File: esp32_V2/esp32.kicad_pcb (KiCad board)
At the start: 2 copper layers, 80 x 64 mm, 75 parts, among them IC1 KF33BD-TR, J1 USB_C, J4 pH, J5 ORP, Q2 8205A, Q3 BC817, Q4 BC817, SW1 Reset, SW2 Boot, U1 CH340G, U2 TC4056, U3 DW01A, U4 LM358, U5 TLC272, U6 LM358, X1 12 MHz

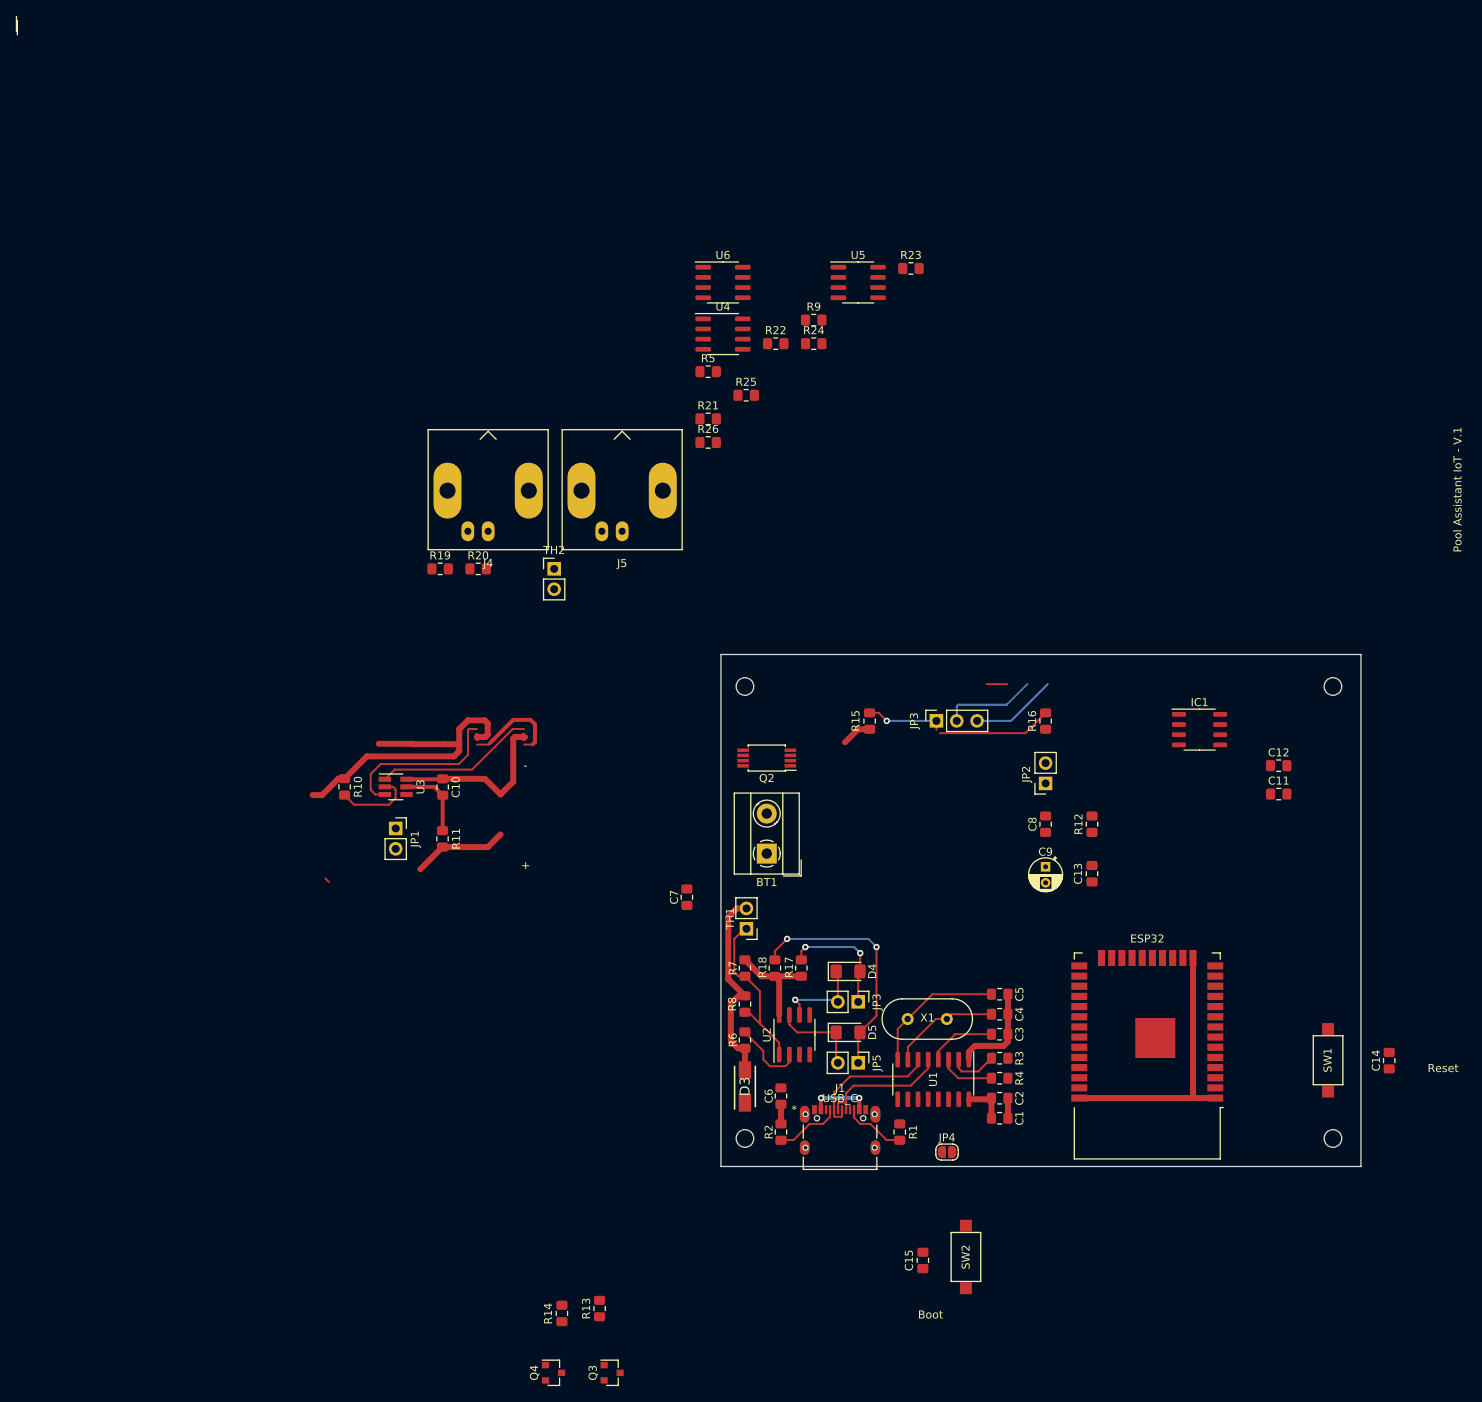
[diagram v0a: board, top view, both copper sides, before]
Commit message: Remove V2 folder and rename V2.1 folder to V2
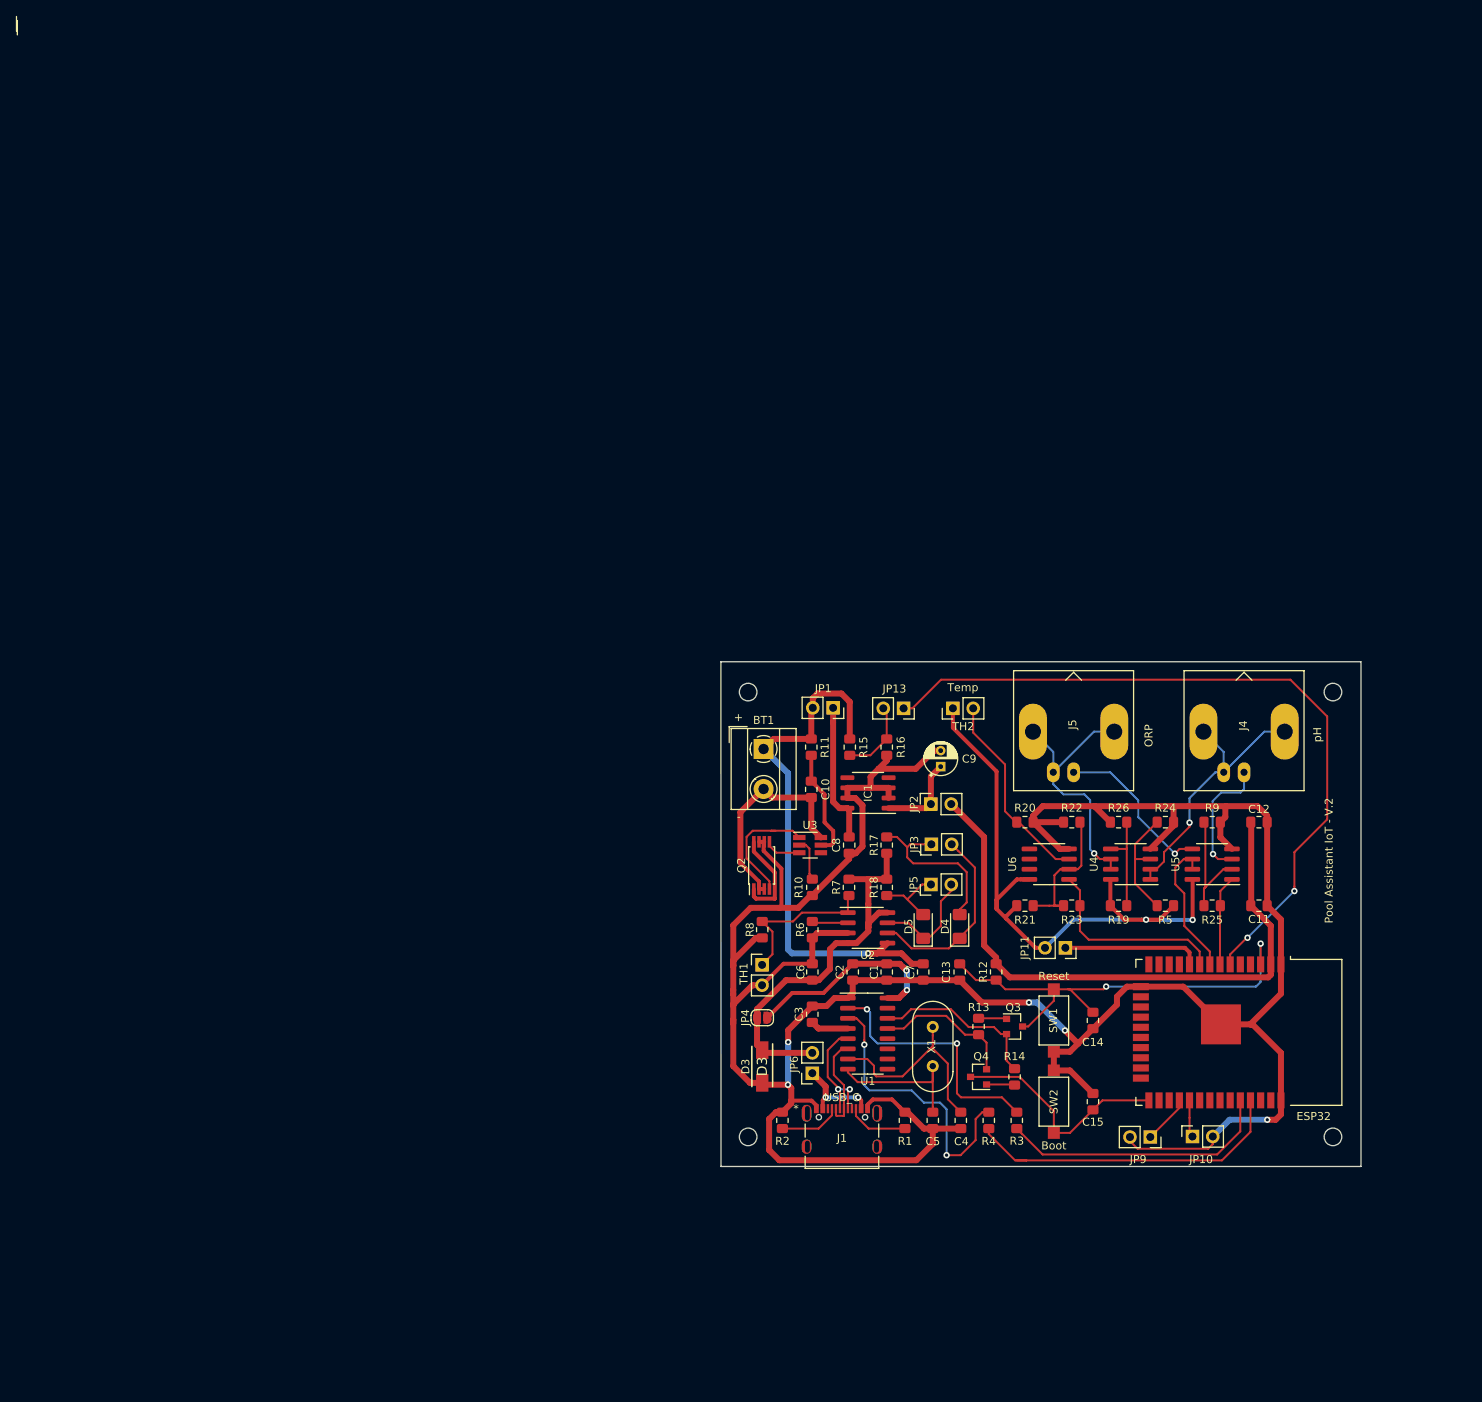
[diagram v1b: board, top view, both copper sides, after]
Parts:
- removed Hole1, Hole3, Hole4: MountingHole_2.2mm_M2_ISO7380, MountingHole:MountingHole_2.2mm_M2_ISO7380
- removed the Hole2 at (164.5, 83.0)
- removed the JP3 at (105.2, 122.4)
- removed the JP3 at (114.9, 87.3)
- added Hole2: MountingHole_2.2mm_M2_ISO7380, MountingHole:MountingHole_2.2mm_M2_ISO7380, F.Cu at (164.5, 83.7)
- added Hole2: MountingHole_2.2mm_M2_ISO7380, MountingHole:MountingHole_2.2mm_M2_ISO7380, F.Cu at (164.5, 139.3)
- added Hole2: MountingHole_2.2mm_M2_ISO7380, MountingHole:MountingHole_2.2mm_M2_ISO7380, F.Cu at (91.4, 139.3)
- added Hole2: MountingHole_2.2mm_M2_ISO7380, MountingHole:MountingHole_2.2mm_M2_ISO7380, F.Cu at (91.4, 83.7)
- added JP10: Jumper_NO, Connector_PinSocket_2.54mm:PinSocket_1x02_P2.54mm_Vertical, F.Cu at (146.9, 139.3)
- added JP11: Jumper_NO, Connector_PinSocket_2.54mm:PinSocket_1x02_P2.54mm_Vertical, F.Cu at (131.1, 115.7)
- added JP13: Jumper_NO, Connector_PinSocket_2.54mm:PinSocket_1x02_P2.54mm_Vertical, F.Cu at (110.8, 85.7)
- added JP3: READY, Connector_PinHeader_2.54mm:PinHeader_1x02_P2.54mm_Vertical, F.Cu at (114.3, 102.7)
- added JP6: Jumper_NO, Connector_PinSocket_2.54mm:PinSocket_1x02_P2.54mm_Vertical, F.Cu at (99.4, 131.3)
- added JP9: Jumper_NO, Connector_PinSocket_2.54mm:PinSocket_1x02_P2.54mm_Vertical, F.Cu at (141.7, 139.3)
- moved J4 99.2 mm to (153.4, 93.7)
- moved R19 94.7 mm to (137.7, 110.4), turned to 180 degrees
- moved R5 87.9 mm to (143.6, 110.4)
- moved R25 86.4 mm to (149.4, 110.4)
- moved U5 85.1 mm to (149.4, 105.2), turned to 180 degrees
- moved U4 83.6 mm to (139.2, 105.2), turned to 180 degrees
- moved U6 83.4 mm to (129.0, 105.2), turned to 180 degrees
- moved R23 82.1 mm to (131.8, 110.4), turned to 180 degrees
- moved R9 80.1 mm to (149.4, 100.0), turned to 180 degrees
- moved R20 75.3 mm to (126.0, 100.0), turned to 180 degrees
- moved R24 74.2 mm to (143.6, 100.0)
- moved R21 72.6 mm to (126.0, 110.4)
- moved R22 70.3 mm to (131.8, 100.0), turned to 180 degrees
- moved R26 69.9 mm to (137.7, 100.0), turned to 180 degrees
- moved G*** 67.0 mm to (151.9, 123.0)
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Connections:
- ESP32 pad 10: Vcc -> Net-(ESP32-Pad10)
- ESP32 pad 6: pH -> Bat
- ESP32 pad 7: Temp -> pH
- ESP32 pad 9: Bat -> Temp
- J1 pad A4-B9: VBUS -> Net-(J1-PadA4-B9)
- J1 pad B4-A9: VBUS -> Net-(J1-PadA4-B9)
- R15 pad 2: Bat -> Net-(JP13-Pad2)
- R16 pad 1: Bat -> Net-(JP13-Pad2)
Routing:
- net GND: track 119.0 -> 370.6 mm, vias 0 -> 5
- net Vcc: track 0.00 -> 81.5 mm, vias 0 -> 2
- net Bat: track 14.3 -> 92.4 mm, vias 0 -> 2
- net +3V3: track 0.00 -> 77.6 mm
- net EN: track 0.00 -> 57.7 mm, vias 0 -> 2
- net Batt+: track 15.6 -> 68.7 mm, vias 0 -> 1
- net Tx: track 0.00 -> 41.4 mm
- net Rx: track 0.00 -> 34.3 mm
- net pH-: track 0.00 -> 34.1 mm, vias 0 -> 1
- net ORP-: track 0.00 -> 33.3 mm, vias 0 -> 1
- net Net-(R4-Pad2): track 6.98 -> 36.2 mm, vias 0 -> 2
- net Boot: track 0.00 -> 28.5 mm
- net VBUS: track 20.7 -> 49.1 mm, vias 2 -> 0
- net Net-(R3-Pad2): track 6.02 -> 31.9 mm, vias 0 -> 2
- net Net-(R20-Pad2): track 0.00 -> 25.0 mm
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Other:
- board size 80 x 64 mm -> 80 x 63.1 mm
- board text added: "D3"
- board text added: "ORP"
- board text added: "Pool Assistant IoT - V.2"
- board text added: "Temp"
- board text added: "pH"
- board text removed: "Pool Assistant IoT - V.1"

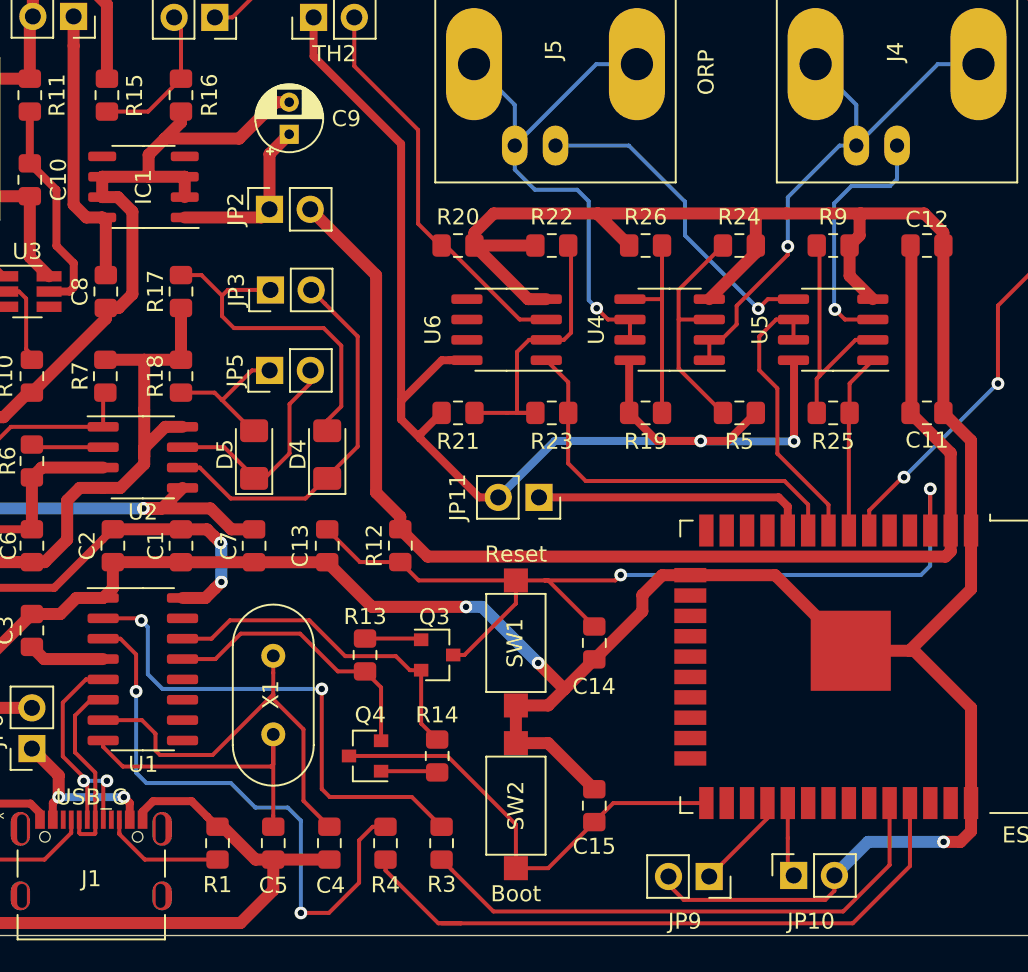
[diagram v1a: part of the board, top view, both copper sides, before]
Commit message: 1) Correct components values in measurement circuits - 2) Schematic cleanup - 3) Fix tracks in PCB - 4) Add Thermistor calculator
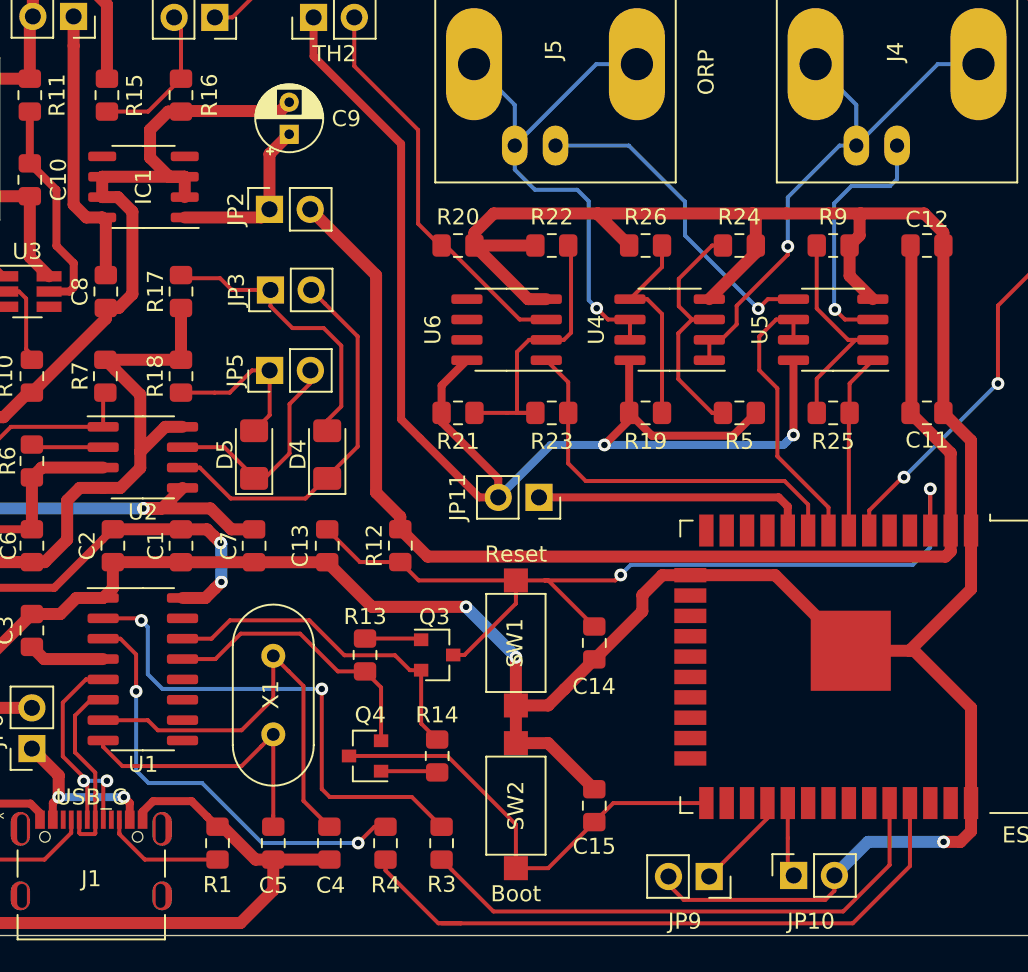
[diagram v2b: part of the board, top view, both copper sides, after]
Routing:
- net Net-(R4-Pad2): track 36.2 -> 27.6 mm
- net Vcc: track 81.5 -> 85.8 mm
- net Net-(D4-Pad2): track 21.5 -> 18.2 mm
- net Net-(R25-Pad1): track 15.1 -> 13.8 mm
- net Net-(C5-Pad1): track 19.2 -> 18.1 mm
- net Net-(D5-Pad2): track 9.33 -> 10.3 mm
- net EN: track 57.7 -> 57.0 mm
- net Net-(R24-Pad1): track 14.6 -> 15.3 mm
- net GND: track 370.6 -> 370.0 mm
- net VBUS: track 49.1 -> 49.7 mm
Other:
- net class Default: clearance 0.25 -> 0.2
- rule trace_clearance: 0.25 -> 0.2
